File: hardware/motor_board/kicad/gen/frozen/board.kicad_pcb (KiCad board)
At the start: 6 copper layers, 85 x 35 mm, 236 parts, among them J1 BOOMELE_1.27-2x10P, J2 WAFER-SH1.0-6PWB, J3 WAFER-SH1.0-6PWB, J4 S5B-XH-A, Q1 HYG015N04LS1C2, Q2 HYG015N04LS1C2, Q3 HYG015N04LS1C2, Q4 HYG015N04LS1C2, Q5 HYG015N04LS1C2, Q6 HYG015N04LS1C2, Q7 HYG015N04LS1C2, Q8 HYG015N04LS1C2, U1 STM32G474RET6, U10 SN74LVC3G17DCUR, U11 TPS22945DCKR, U12 TPS22945DCKR, U13 LM74502DDFR, U14 74LVC1G17SE-7, U2 DRV8323RHRGZR, U3 DRV8316CRRGFR, U4 DRV8316CRRGFR, U5 AP2112K-3.3TRG1, U6 SN74LVC08APWR, U7 INA239AIDGSR, U8 BQ76907RGRR, U9 SN74LVC3G17DCUR

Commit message: tail: C46 flipped to the bottom (GND pad off an unanchored F fill island); DRC 0, parity 0, 17 open
Co-Authored-By: Claude Opus 5.5 (1M context) <noreply@anthropic.com>
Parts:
- C46: moved to B.Cu
- moved C46 0.56 mm to (143.1, 93.6), turned to 90 degrees
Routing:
- net GND: track 216.6 -> 215.7 mm
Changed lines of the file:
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@@
 		)
 	)
-	(footprint "Capacitor_SMD:C_0402_1005Metric"
-		(layer "F.Cu")
-		(at 142.85 94.1)
-		(descr "Capacitor SMD 0402 (1005 Metric), square (rectangular) end terminal, IPC-7351 nominal, (Body size source: IPC-SM-782 page 76, https://www.pcb-3d.com/wordpress/wp-content/uploads/ipc-sm-782a_amendment_1_and_2.pdf)")
-		(tags "capacitor")
-		(property "Reference" "C46"
-			(at 0 -1.16 180)
-			(layer "F.SilkS")
-			(effects
-				(font
-					(size 0.8 0.8)
-					(thickness 0.12)
-				)
-			)
-		)
-		(property "Value" "1uF 25V"
-			(at 0 1.16 180)
-			(layer "F.Fab")
-			(hide yes)
-			(effects
-				(font
-					(size 1 1)
-					(thickness 0.15)
-				)
-			)
-		)
-		(property "Datasheet" ""
-			(at 0 0 180)
-			(layer "F.Fab")
-			(hide yes)
-			(effects
-				(font
-					(size 1.27 1.27)
-				)
-			)
-		)
-		(property "Description" "Unpolarized capacitor"
-			(at 0 0 180)
-			(layer "F.Fab")
-			(hide yes)
-			(effects
-				(font
-					(size 1.27 1.27)
-				)
-			)
-		)
-		(property "KiLib_Generator" "SMD_2terminal_chip_molded"
-			(at 0 0 180)
-			(layer "F.SilkS")
-			(hide yes)
-			(effects
-				(font
-					(size 1 1)
-					(thickness 0.15)
-				)
-			)
-		)
-		(property "LCSC" "C52923"
-			(at 0 0 180)
-			(layer "F.SilkS")
-			(hide yes)
-			(effects
-				(font
-					(size 1.27 1.27)
-					(thickness 0.15)
-				)
-			)
-		)
-		(sheetname "sensors")
-		(sheetfile "sensors.kicad_sch")
-		(attr smd)
-		(duplicate_pad_numbers_are_jumpers no)
-		(fp_line
-			(start -0.107836 -0.36)
-			(end 0.107836 -0.36)
-			(stroke
-				(width 0.12)
-				(type solid)
-			)
-			(layer "F.SilkS")
-		)
-		(fp_line
-			(start -0.107836 0.36)
-			(end 0.107836 0.36)
-			(stroke
-				(width 0.12)
-				(type solid)
-			)
-			(layer "F.SilkS")
-		)
-		(fp_rect
-			(start -0.91 -0.46)
-			(end 0.91 0.46)
-			(stroke
-				(width 0.05)
-				(type solid)
-			)
-			(fill no)
-			(layer "F.CrtYd")
-		)
-		(fp_rect
-			(start -0.5 -0.25)
-			(end 0.5 0.25)
-			(stroke
-				(width 0.1)
-				(type solid)
-			)
-			(fill no)
-			(layer "F.Fab")
-		)
-		(fp_text user "${REFERENCE}"
-			(at 0 0 180)
-			(layer "F.Fab")
-			(effects
-				(font
-					(size 0.25 0.25)
-					(thickness 0.04)
-				)
-			)
-		)
-		(pad "1" smd roundrect
-			(at -0.48 0)
-			(size 0.56 0.62)
-			(layers "F.Cu" "F.Mask" "F.Paste")
-			(roundrect_rratio 0.25)
-			(net "/sensors/L_VS")
-		)
-		(pad "2" smd roundrect
-			(at 0.48 0)
-			(size 0.56 0.62)
-			(layers "F.Cu" "F.Mask" "F.Paste")
-			(roundrect_rratio 0.25)
-			(net "GND")
-		)
-		(embedded_fonts no)
-		(model "${KICAD10_3DMODEL_DIR}/Capacitor_SMD.3dshapes/C_0402_1005Metric.step"
-			(offset
-				(xyz 0 0 0)
-			)
-			(scale
-				(xyz 1 1 1)
-			)
-			(rotate
-				(xyz 0 0 0)
-			)
-		)
-	)
 	(footprint "Capacitor_SMD:C_0603_1608Metric"
 		(layer "F.Cu")
@@
 		)
 	)
+	(footprint "Capacitor_SMD:C_0402_1005Metric"
+		(layer "B.Cu")
+		(at 143.1 93.6 90)
+		(descr "Capacitor SMD 0402 (1005 Metric), square (rectangular) end terminal, IPC-7351 nominal, (Body size source: IPC-SM-782 page 76, https://www.pcb-3d.com/wordpress/wp-content/uploads/ipc-sm-782a_amendment_1_and_2.pdf)")
+		(tags "capacitor")
+		(property "Reference" "C46"
+			(at 0 1.16 270)
+			(layer "B.SilkS")
+			(effects
+				(font
+					(size 0.8 0.8)
+					(thickness 0.12)
+				)
+				(justify mirror)
+			)
+		)
+		(property "Value" "1uF 25V"
+			(at 0 -1.16 270)
+			(layer "B.Fab")
+			(hide yes)
+			(effects
+				(font
+					(size 1 1)
+					(thickness 0.15)
+				)
+				(justify mirror)
+			)
+		)
+		(property "Datasheet" ""
+			(at 0 0 270)
+			(layer "B.Fab")
+			(hide yes)
+			(effects
+				(font
+					(size 1.27 1.27)
+				)
+				(justify mirror)
+			)
+		)
+		(property "Description" "Unpolarized capacitor"
+			(at 0 0 270)
+			(layer "B.Fab")
+			(hide yes)
+			(effects
+				(font
+					(size 1.27 1.27)
+				)
+				(justify mirror)
+			)
+		)
+		(property "KiLib_Generator" "SMD_2terminal_chip_molded"
+			(at 0 0 270)
+			(layer "B.SilkS")
+			(hide yes)
+			(effects
+				(font
+					(size 1 1)
+					(thickness 0.15)
+				)
+				(justify mirror)
+			)
+		)
+		(property "LCSC" "C52923"
+			(at 0 0 270)
+			(layer "B.SilkS")
+			(hide yes)
+			(effects
+				(font
+					(size 1.27 1.27)
+					(thickness 0.15)
+				)
+				(justify mirror)
+			)
+		)
+		(sheetname "sensors")
+		(sheetfile "sensors.kicad_sch")
+		(attr smd)
+		(duplicate_pad_numbers_are_jumpers no)
+		(fp_line
+			(start -0.107836 -0.36)
+			(end 0.107836 -0.36)
+			(stroke
+				(width 0.12)
+				(type solid)
+			)
+			(layer "B.SilkS")
+		)
+		(fp_line
+			(start -0.107836 0.36)
+			(end 0.107836 0.36)
+			(stroke
+				(width 0.12)
+				(type solid)
+			)
+			(layer "B.SilkS")
+		)
+		(fp_rect
+			(start -0.91 0.46)
+			(end 0.91 -0.46)
+			(stroke
+				(width 0.05)
+				(type solid)
+			)
+			(fill no)
+			(layer "B.CrtYd")
+		)
+		(fp_rect
+			(start -0.5 0.25)
+			(end 0.5 -0.25)
+			(stroke
+				(width 0.1)
+				(type solid)
+			)
+			(fill no)
+			(layer "B.Fab")
+		)
+		(fp_text user "${REFERENCE}"
+			(at 0 0 270)
+			(layer "B.Fab")
+			(effects
+				(font
+					(size 0.25 0.25)
+					(thickness 0.04)
+				)
+				(justify mirror)
+			)
+		)
+		(pad "1" smd roundrect
+			(at -0.48 0 90)
+			(size 0.56 0.62)
+			(layers "B.Cu" "B.Mask" "B.Paste")
+			(roundrect_rratio 0.25)
+			(net "/sensors/L_VS")
+		)
+		(pad "2" smd roundrect
+			(at 0.48 0 90)
+			(size 0.56 0.62)
+			(layers "B.Cu" "B.Mask" "B.Paste")
+			(roundrect_rratio 0.25)
+			(net "GND")
+		)
+		(embedded_fonts no)
+		(model "${KICAD10_3DMODEL_DIR}/Capacitor_SMD.3dshapes/C_0402_1005Metric.step"
+			(offset
+				(xyz 0 0 0)
+			)
+			(scale
+				(xyz 1 1 1)
+			)
+			(rotate
+				(xyz 0 0 0)
+			)
+		)
+	)
 	(footprint "Resistor_SMD:R_1206_3216Metric"
 		(layer "B.Cu")
@@
 		(width 0.2)
 		(layer "F.Cu")
-		(net "GND")
-	)
-	(segment
-		(start 143.329999 94.1)
-		(end 144.2 94.1)
-		(width 0.2)
-		(layer "F.Cu")

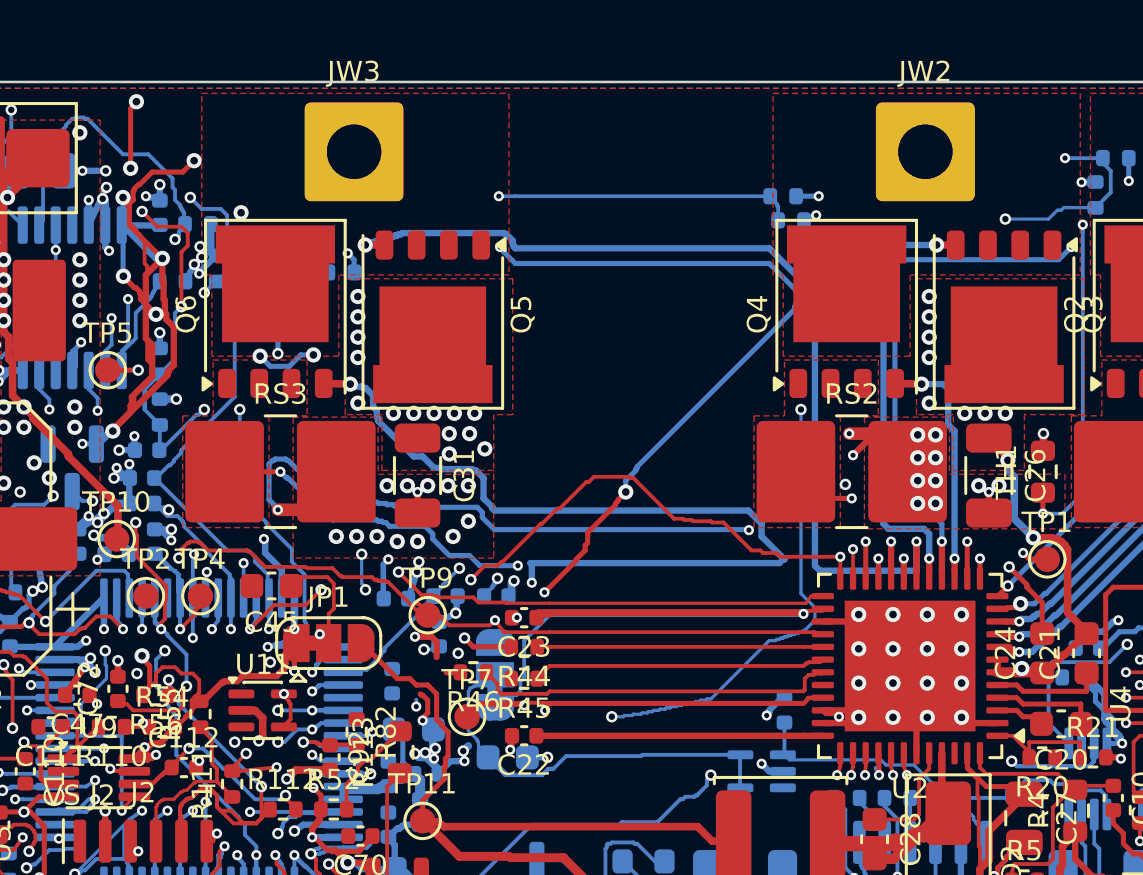
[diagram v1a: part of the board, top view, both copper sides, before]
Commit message: tail: weapon cell C moved +10 mm back beside cell B (undoes the grow's split; its gate/sense copper restored from the pre-grow board); free area now at U1's north side; DRC 0, parity 0, 17 open
Co-Authored-By: Claude Opus 5.5 (1M context) <noreply@anthropic.com>
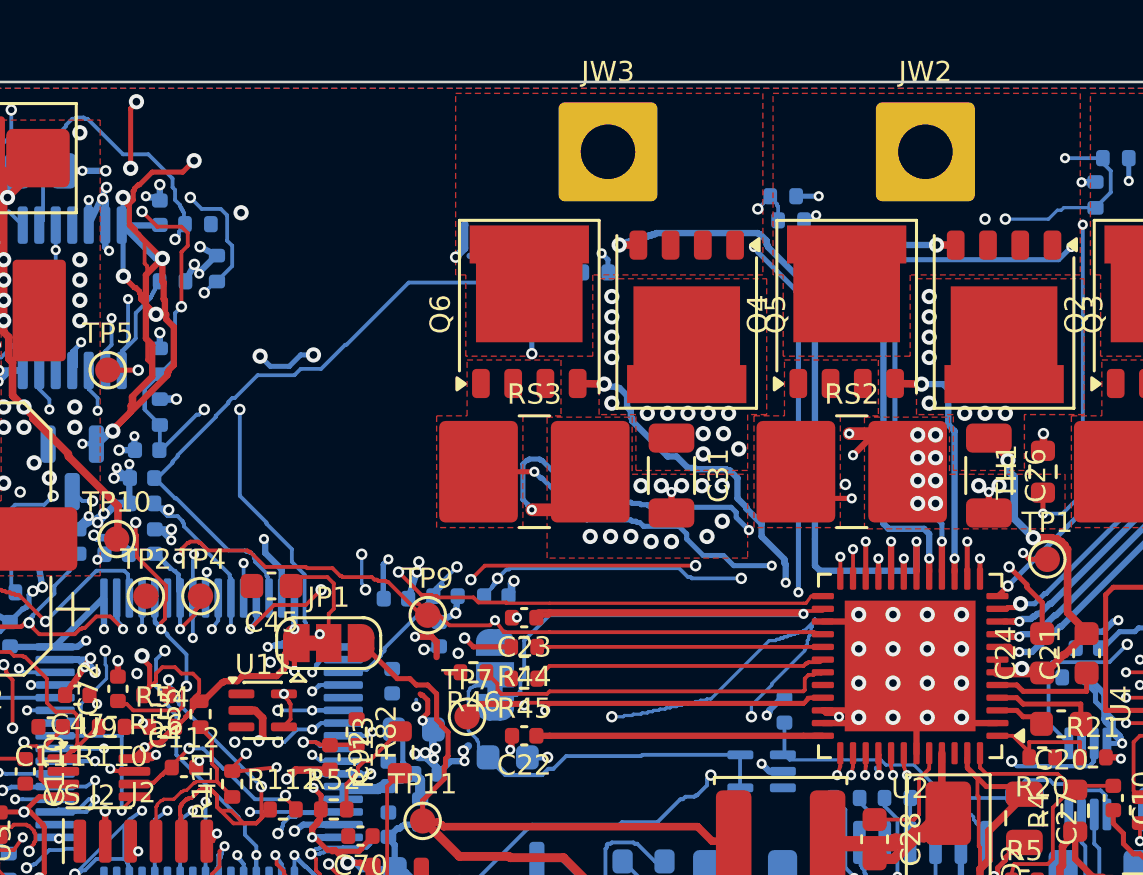
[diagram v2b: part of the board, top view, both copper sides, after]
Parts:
- moved C31 10.0 mm to (154.1, 85.5)
- moved JW3 10.0 mm to (151.6, 72.8)
- moved NT3 10.0 mm to (149.1, 86.8)
- moved Q5 10.0 mm to (154.7, 79.2)
- moved Q6 10.0 mm to (148.5, 79.1)
- moved R26 10.0 mm to (151.1, 77.5)
- moved R27 10.0 mm to (148.2, 77.8)
- moved RS3 10.0 mm to (148.7, 85.3)
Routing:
- net /weapon/W_GLC: track 50.0 -> 20.1 mm
- net W_VB: track 53.9 -> 28.2 mm
- net /weapon/W_C: track 45.3 -> 21.1 mm, vias 5 -> 4
- net /weapon/W_GHC: track 36.9 -> 26.9 mm
- net /weapon/W_SNC: track 28.2 -> 18.2 mm
- net /weapon/W_SLC: track 27.0 -> 17.0 mm
- net W_VA: track 63.6 -> 73.0 mm, vias 6 -> 7
- net W_SOB: track 36.4 -> 28.6 mm, vias 4 -> 5
- net W_VC: track 21.0 -> 27.6 mm, vias 1 -> 0
- net W_NTC: track 74.5 -> 72.8 mm, vias 6 -> 7
- net W_SOC: vias 4 -> 10
- net GND: vias 274 -> 268
